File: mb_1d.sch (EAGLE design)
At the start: 57 parts, among them CON1 1013279X_AMPHENOL_2X25, CON2 1013279X_AMPHENOL_2X25, U1 TPS61040, U10 TPS610981, U2 MAX5394, U3 TPS61040, U4 74HC4050, U5 RFD77101, U6 MAX5394, U7 MAX5026EUT+T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

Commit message: Began schematic
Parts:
- added U9: HEADER_5X2_SMD_1.27MM, ck:HEADER_5X2_SMD_1.27MM
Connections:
- new net AIN2: U5.P0.01/AIN2, U9.P10
- new net AREF0: U5.P0.00/AREF0, U9.P9
- net 3.3V: now also U9.P7
- net GND: now also U9.P1
- net RESET: now also U9.P8
- net SS_POT1: now also U5.P0.07
- net SS_POT2: now also U5.P0.10
- net SS_POT3: now also U5.P0.13
- net TX_EN_M: now also U9.P2
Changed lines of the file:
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@@
 <part name="U8" library="ck" deviceset="MAX5394" device=""/>
 <part name="R13" library="SparkFun-Resistors" deviceset="RESISTOR" device="0402" value="50k"/>
+<part name="U9" library="ck" deviceset="HEADER_5X2_SMD_1.27MM" device=""/>
 </parts>
 <sheets>
@@
 <instance part="U8" gate="U1" x="-95.25" y="-35.56"/>
 <instance part="R13" gate="G$1" x="-80.01" y="-49.53" rot="R90"/>
+<instance part="U9" gate="U1" x="29.21" y="-64.77"/>
 </instances>
 <busses>
@@
 <label x="-80.01" y="-59.69" size="1.778" layer="95"/>
 </segment>
+<segment>
+<pinref part="U9" gate="U1" pin="P1"/>
+<wire x1="21.59" y1="-58.42" x2="13.97" y2="-58.42" width="0.1524" layer="91"/>
+<label x="13.97" y="-58.42" size="1.778" layer="95"/>
+</segment>
 </net>
 <net name="3.3V" class="0">
@@
 <label x="-113.03" y="-27.94" size="1.778" layer="95"/>
 </segment>
+<segment>
+<pinref part="U9" gate="U1" pin="P7"/>
+<wire x1="36.83" y1="-66.04" x2="45.72" y2="-66.04" width="0.1524" layer="91"/>
+<label x="40.64" y="-66.04" size="1.778" layer="95"/>
+</segment>
 </net>
 <net name="SCK" class="0">
@@
 <pinref part="CON2" gate="CON1" pin="P$41"/>
 </segment>
+<segment>
+<pinref part="U9" gate="U1" pin="P2"/>
+<wire x1="21.59" y1="-60.96" x2="13.97" y2="-60.96" width="0.1524" layer="91"/>
+<label x="10.16" y="-60.96" size="1.778" layer="95"/>
+</segment>
 </net>
 <net name="RSTB_M" class="0">
@@
 <wire x1="90.17" y1="-62.23" x2="83.82" y2="-62.23" width="0.1524" layer="91"/>
 <label x="83.82" y="-62.23" size="1.778" layer="95"/>
+</segment>
+<segment>
+<pinref part="U9" gate="U1" pin="P8"/>
+<wire x1="36.83" y1="-63.5" x2="45.72" y2="-63.5" width="0.1524" layer="91"/>
+<label x="40.64" y="-63.5" size="1.778" layer="95"/>
 </segment>
 </net>
@@
 <label x="12.7" y="25.4" size="1.778" layer="95"/>
 </segment>
+<segment>
+<pinref part="U5" gate="G$1" pin="P0.07"/>
+<wire x1="125.73" y1="-107.95" x2="125.73" y2="-114.3" width="0.1524" layer="91"/>
+<label x="125.73" y="-119.38" size="1.778" layer="95" rot="R90"/>
+</segment>
 </net>
 <net name="SS_POT2" class="0">
@@
 <wire x1="-224.79" y1="-36.83" x2="-233.68" y2="-36.83" width="0.1524" layer="91"/>
 <label x="-237.49" y="-36.83" size="1.778" layer="95"/>
+</segment>
+<segment>
+<pinref part="U5" gate="G$1" pin="P0.10"/>
+<wire x1="128.27" y1="-107.95" x2="128.27" y2="-114.3" width="0.1524" layer="91"/>
+<label x="128.27" y="-119.38" size="1.778" layer="95" rot="R90"/>
 </segment>
 </net>
@@
 <label x="-118.11" y="-33.02" size="1.778" layer="95"/>
 </segment>
+<segment>
+<pinref part="U5" gate="G$1" pin="P0.13"/>
+<wire x1="130.81" y1="-107.95" x2="130.81" y2="-114.3" width="0.1524" layer="91"/>
+<label x="130.81" y="-119.38" size="1.778" layer="95" rot="R90"/>
+</segment>
 </net>
 <net name="MOSI_LS" class="0">
@@
 </segment>
 </net>
+<net name="AIN2" class="0">
+<segment>
+<pinref part="U9" gate="U1" pin="P10"/>
+<wire x1="36.83" y1="-58.42" x2="45.72" y2="-58.42" width="0.1524" layer="91"/>
+<label x="41.91" y="-58.42" size="1.778" layer="95"/>
+</segment>
+<segment>
+<pinref part="U5" gate="G$1" pin="P0.01/AIN2"/>
+<wire x1="118.11" y1="-107.95" x2="118.11" y2="-114.3" width="0.1524" layer="91"/>
+<label x="118.11" y="-114.3" size="1.778" layer="95" rot="R90"/>
+</segment>
+</net>
+<net name="AREF0" class="0">
+<segment>
+<pinref part="U9" gate="U1" pin="P9"/>
+<wire x1="36.83" y1="-60.96" x2="45.72" y2="-60.96" width="0.1524" layer="91"/>
+<label x="40.64" y="-60.96" size="1.778" layer="95"/>
+</segment>
+<segment>
+<pinref part="U5" gate="G$1" pin="P0.00/AREF0"/>
+<wire x1="123.19" y1="-107.95" x2="123.19" y2="-114.3" width="0.1524" layer="91"/>
+<label x="123.19" y="-114.3" size="1.778" layer="95" rot="R90"/>
+</segment>
+</net>

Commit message: Fixed errors
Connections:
- removed net N$5: D3.C, D4.A
- removed net N$6: D4.C, D5.A
- net 3.3V: now also U5.VDD
- net GND: now also U5.GND@1, U5.GND@42, U5.GND@44, U5.GND@45
- net N$10: now also D6.C, R3.1; no longer D5.C, D6.A
- net N$4: now also D3.C, D4.A
- net N$7: now also D4.C, D5.A
- net N$9: now also D5.C, D6.A
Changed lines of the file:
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@@
 <setting verticaltext="up"/>
 </settings>
-<grid distance="0.05" unitdist="inch" unit="inch" style="lines" multiple="1" display="no" altdistance="0.01" altunitdist="inch" altunit="inch"/>
+<grid distance="0.1" unitdist="inch" unit="inch" style="lines" multiple="1" display="no" altdistance="0.01" altunitdist="inch" altunit="inch"/>
 <layers>
 <layer number="1" name="Top" color="4" fill="1" visible="no" active="no"/>
@@
 </segment>
 <segment>
-<wire x1="91.44" y1="-44.45" x2="83.82" y2="-44.45" width="0.1524" layer="91"/>
-<label x="85.09" y="-44.45" size="1.778" layer="95"/>
-</segment>
-<segment>
 <pinref part="U5" gate="G$1" pin="GND@2"/>
 <wire x1="90.17" y1="-46.99" x2="83.82" y2="-46.99" width="0.1524" layer="91"/>
@@
 </segment>
 <segment>
-<wire x1="105.41" y1="-106.68" x2="105.41" y2="-114.3" width="0.1524" layer="91"/>
-<label x="105.41" y="-113.03" size="1.778" layer="95" rot="R90"/>
-</segment>
-<segment>
 <pinref part="U5" gate="G$1" pin="GND@43"/>
 <wire x1="107.95" y1="-107.95" x2="107.95" y2="-114.3" width="0.1524" layer="91"/>
 <label x="107.95" y="-113.03" size="1.778" layer="95" rot="R90"/>
-</segment>
-<segment>
-<wire x1="135.89" y1="-106.68" x2="135.89" y2="-114.3" width="0.1524" layer="91"/>
-<label x="135.89" y="-113.03" size="1.778" layer="95" rot="R90"/>
-</segment>
-<segment>
-<wire x1="138.43" y1="-106.68" x2="138.43" y2="-114.3" width="0.1524" layer="91"/>
-<label x="138.43" y="-113.03" size="1.778" layer="95" rot="R90"/>
 </segment>
 <segment>
@@
 <label x="13.97" y="-58.42" size="1.778" layer="95"/>
 </segment>
+<segment>
+<pinref part="U5" gate="G$1" pin="GND@1"/>
+<wire x1="90.17" y1="-44.45" x2="83.82" y2="-44.45" width="0.1524" layer="91"/>
+<label x="85.09" y="-44.45" size="1.778" layer="95"/>
+</segment>
+<segment>
+<pinref part="U5" gate="G$1" pin="GND@42"/>
+<wire x1="105.41" y1="-107.95" x2="105.41" y2="-114.3" width="0.1524" layer="91"/>
+<label x="105.41" y="-113.03" size="1.778" layer="95" rot="R90"/>
+</segment>
+<segment>
+<pinref part="U5" gate="G$1" pin="GND@44"/>
+<wire x1="135.89" y1="-107.95" x2="135.89" y2="-114.3" width="0.1524" layer="91"/>
+<label x="135.89" y="-114.3" size="1.778" layer="95" rot="R90"/>
+</segment>
+<segment>
+<pinref part="U5" gate="G$1" pin="GND@45"/>
+<wire x1="138.43" y1="-107.95" x2="138.43" y2="-114.3" width="0.1524" layer="91"/>
+<label x="138.43" y="-114.3" size="1.778" layer="95" rot="R90"/>
+</segment>
 </net>
 <net name="3.3V" class="0">
@@
 <junction x="-292.1" y="-29.21"/>
 <label x="-295.91" y="-29.21" size="1.778" layer="95"/>
-</segment>
-<segment>
-<wire x1="91.44" y1="-59.69" x2="83.82" y2="-59.69" width="0.1524" layer="91"/>
-<label x="83.82" y="-59.69" size="1.778" layer="95"/>
 </segment>
 <segment>
@@
 <label x="40.64" y="-66.04" size="1.778" layer="95"/>
 </segment>
+<segment>
+<pinref part="U5" gate="G$1" pin="VDD"/>
+<wire x1="90.17" y1="-59.69" x2="83.82" y2="-59.69" width="0.1524" layer="91"/>
+<label x="85.09" y="-59.69" size="1.778" layer="95"/>
+</segment>
 </net>
 <net name="SCK" class="0">
@@
 </segment>
 </net>
-<net name="N$4" class="0">
-<segment>
-<pinref part="C7" gate="G$1" pin="2"/>
-<wire x1="-134.62" y1="31.75" x2="-134.62" y2="30.48" width="0.1524" layer="91"/>
-</segment>
-</net>
 <net name="N$7" class="0">
 <segment>
@@
 <wire x1="-115.57" y1="22.86" x2="-125.73" y2="22.86" width="0.1524" layer="91"/>
 <junction x="-125.73" y="22.86"/>
-</segment>
-</net>
-<net name="N$9" class="0">
-<segment>
-<pinref part="C9" gate="G$1" pin="2"/>
-<wire x1="-114.3" y1="31.75" x2="-114.3" y2="30.48" width="0.1524" layer="91"/>
+<pinref part="D4" gate="G$1" pin="C"/>
+<wire x1="-128.27" y1="30.48" x2="-125.73" y2="30.48" width="0.1524" layer="91"/>
+<pinref part="D5" gate="G$1" pin="A"/>
+<wire x1="-125.73" y1="30.48" x2="-123.19" y2="30.48" width="0.1524" layer="91"/>
+<junction x="-125.73" y="30.48"/>
 </segment>
 </net>
@@
 </segment>
 </net>
-<net name="N$5" class="0">
-<segment>
-<pinref part="D3" gate="G$1" pin="C"/>
-<pinref part="D4" gate="G$1" pin="A"/>
-<wire x1="-138.43" y1="30.48" x2="-133.35" y2="30.48" width="0.1524" layer="91"/>
-</segment>
-</net>
-<net name="N$6" class="0">
-<segment>
-<pinref part="D4" gate="G$1" pin="C"/>
-<pinref part="D5" gate="G$1" pin="A"/>
-<wire x1="-128.27" y1="30.48" x2="-123.19" y2="30.48" width="0.1524" layer="91"/>
-</segment>
-</net>
-<net name="N$10" class="0">
-<segment>
-<pinref part="D5" gate="G$1" pin="C"/>
-<pinref part="D6" gate="G$1" pin="A"/>
-<wire x1="-118.11" y1="30.48" x2="-113.03" y2="30.48" width="0.1524" layer="91"/>
-</segment>
-</net>
 <net name="N$12" class="0">
 <segment>
@@
 </segment>
 </net>
+<net name="N$9" class="0">
+<segment>
+<pinref part="D5" gate="G$1" pin="C"/>
+<pinref part="D6" gate="G$1" pin="A"/>
+<wire x1="-118.11" y1="30.48" x2="-114.3" y2="30.48" width="0.1524" layer="91"/>
+<pinref part="C9" gate="G$1" pin="2"/>
+<wire x1="-114.3" y1="30.48" x2="-113.03" y2="30.48" width="0.1524" layer="91"/>
+<wire x1="-114.3" y1="31.75" x2="-114.3" y2="30.48" width="0.1524" layer="91"/>
+<junction x="-114.3" y="30.48"/>
+</segment>
+</net>
+<net name="N$10" class="0">
+<segment>
+<pinref part="D6" gate="G$1" pin="C"/>
+<pinref part="R3" gate="G$1" pin="1"/>
+<wire x1="-107.95" y1="30.48" x2="-106.68" y2="30.48" width="0.1524" layer="91"/>
+</segment>
+</net>
+<net name="N$4" class="0">
+<segment>
+<pinref part="D3" gate="G$1" pin="C"/>
+<pinref part="C7" gate="G$1" pin="2"/>
+<wire x1="-138.43" y1="30.48" x2="-134.62" y2="30.48" width="0.1524" layer="91"/>
+<wire x1="-134.62" y1="30.48" x2="-134.62" y2="31.75" width="0.1524" layer="91"/>
+<pinref part="D4" gate="G$1" pin="A"/>
+<wire x1="-134.62" y1="30.48" x2="-133.35" y2="30.48" width="0.1524" layer="91"/>
+<junction x="-134.62" y="30.48"/>
+</segment>
+</net>

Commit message: Added LQH3NPN470MJRL to schematic
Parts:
- removed L2: CR32, inductors:CR32
- added C17: 470nF, SparkFun-Capacitors:470NF-0402-16V-10%
- added U$2: (no value), Personal:LQH3NPN470MJRL
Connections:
- removed net HVCMUT: R8.1, U$1.OUT
- net 3.3V: now also U$2.1; no longer L2.1
- net CLK_CP: now also U9.P4
- net GND: now also C17.1
- net HVDC: now also C17.2, R8.1, U$1.OUT
- net N$8: now also U$2.2; no longer L2.2
- net OUT16_BUF: now also U9.P5
- net REF_CLK: now also U9.P3
- net REF_CLK_BUF: now also U9.P6
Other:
- moved on the sheet: U4, U9

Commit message: Routed Simblee
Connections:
- net CLK_CP: now also U5.P0.11; no longer U5.P0.04/AIN5
- net RSTB_M: now also U5.P0.09; no longer U5.P0.06/AREF1/AIN7
- net SS_POT1: now also U5.P0.16; no longer U5.P0.07
- net SS_POT2: now also U5.P0.15; no longer U5.P0.10
- net SS_POT3: now also U5.P0.12; no longer U5.P0.13
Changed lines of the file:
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@@
 </variantdefs>
 <classes>
-<class number="0" name="default" width="0" drill="0">
+<class number="0" name="default" width="0.1524" drill="0.254">
+<clearance class="0" value="0.1524"/>
 </class>
 </classes>
@@
 </segment>
 <segment>
-<pinref part="U5" gate="G$1" pin="P0.04/AIN5"/>
-<wire x1="153.67" y1="-85.09" x2="162.56" y2="-85.09" width="0.1524" layer="91"/>
-<label x="154.94" y="-85.09" size="1.778" layer="95"/>
-</segment>
-<segment>
 <pinref part="U9" gate="U1" pin="P4"/>
 <wire x1="115.57" y1="7.62" x2="107.95" y2="7.62" width="0.1524" layer="91"/>
 <label x="105.41" y="7.62" size="1.778" layer="95"/>
+</segment>
+<segment>
+<pinref part="U5" gate="G$1" pin="P0.11"/>
+<wire x1="90.17" y1="-85.09" x2="83.82" y2="-85.09" width="0.1524" layer="91"/>
+<label x="80.01" y="-85.09" size="1.778" layer="95"/>
 </segment>
 </net>
@@
 </segment>
 <segment>
-<pinref part="U5" gate="G$1" pin="P0.06/AREF1/AIN7"/>
-<wire x1="153.67" y1="-87.63" x2="162.56" y2="-87.63" width="0.1524" layer="91"/>
-<label x="154.94" y="-87.63" size="1.778" layer="95"/>
+<pinref part="U5" gate="G$1" pin="P0.09"/>
+<wire x1="90.17" y1="-87.63" x2="83.82" y2="-87.63" width="0.1524" layer="91"/>
+<label x="81.28" y="-87.63" size="1.778" layer="95"/>
 </segment>
 </net>
@@
 </segment>
 <segment>
-<pinref part="U5" gate="G$1" pin="P0.07"/>
-<wire x1="125.73" y1="-107.95" x2="125.73" y2="-114.3" width="0.1524" layer="91"/>
-<label x="125.73" y="-119.38" size="1.778" layer="95" rot="R90"/>
+<pinref part="U5" gate="G$1" pin="P0.16"/>
+<wire x1="90.17" y1="-77.47" x2="83.82" y2="-77.47" width="0.1524" layer="91"/>
+<label x="80.01" y="-77.47" size="1.778" layer="95"/>
 </segment>
 </net>
@@
 </segment>
 <segment>
-<pinref part="U5" gate="G$1" pin="P0.10"/>
-<wire x1="128.27" y1="-107.95" x2="128.27" y2="-114.3" width="0.1524" layer="91"/>
-<label x="128.27" y="-119.38" size="1.778" layer="95" rot="R90"/>
+<pinref part="U5" gate="G$1" pin="P0.15"/>
+<wire x1="90.17" y1="-80.01" x2="83.82" y2="-80.01" width="0.1524" layer="91"/>
+<label x="80.01" y="-80.01" size="1.778" layer="95"/>
 </segment>
 </net>
@@
 </segment>
 <segment>
-<pinref part="U5" gate="G$1" pin="P0.13"/>
-<wire x1="130.81" y1="-107.95" x2="130.81" y2="-114.3" width="0.1524" layer="91"/>
-<label x="130.81" y="-119.38" size="1.778" layer="95" rot="R90"/>
-</segment>
-</net>
+<pinref part="U5" gate="G$1" pin="P0.12"/>
+<wire x1="90.17" y1="-82.55" x2="83.82" y2="-82.55" width="0.1524" layer="91"/>
+<label x="81.28" y="-82.55" size="1.778" layer="95"/>
+</segment>
+</net>

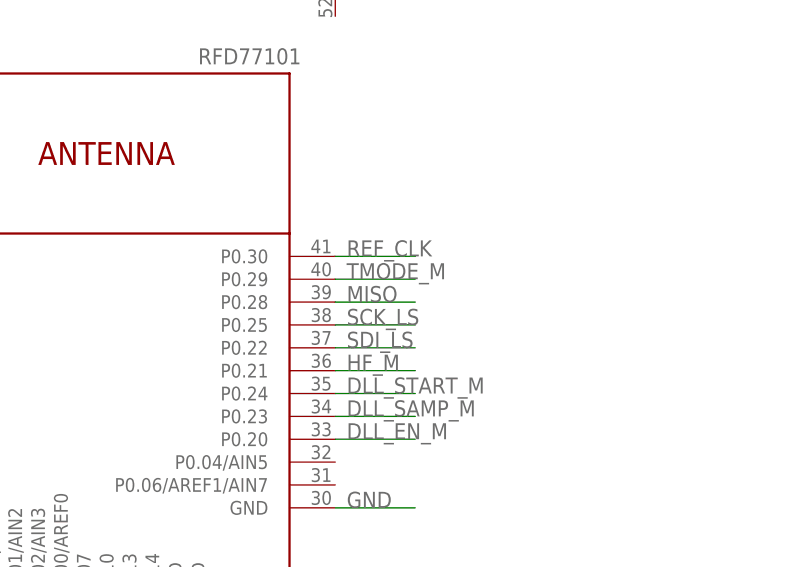
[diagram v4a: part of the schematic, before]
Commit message: Updated Simblee routes
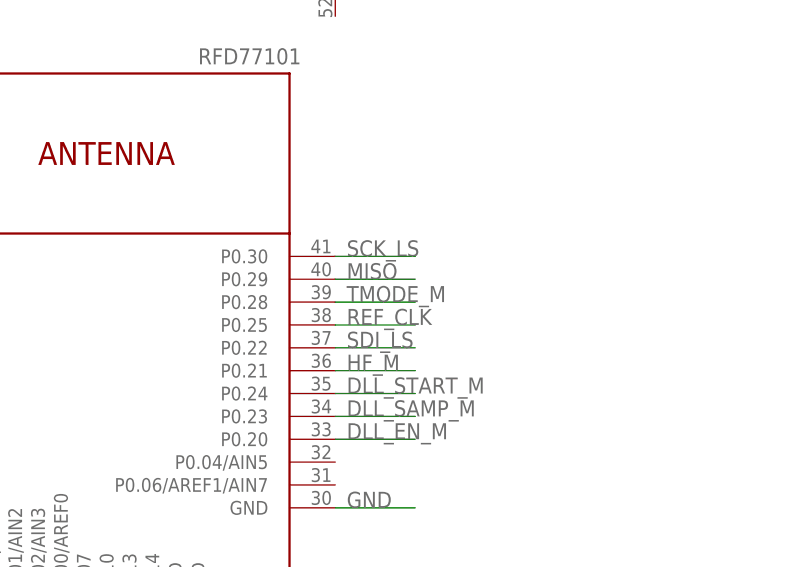
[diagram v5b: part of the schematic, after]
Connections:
- net MISO: now also U5.P0.29; no longer U5.P0.28
- net REF_CLK: now also U5.P0.25; no longer U5.P0.30
- net SCK_LS: now also U5.P0.30; no longer U5.P0.25
- net TMODE_M: now also U5.P0.28; no longer U5.P0.29

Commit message: First version of completed routing
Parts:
- removed D2: ZHCS1000, zetex:ZHCS1000
- removed U4: 74HC4050, ck:74HC4050
- added U$3: (no value), Personal:SN74AUP2G34DCKR
- added U$4: (no value), Personal:DB2J40700L
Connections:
- removed net MOSI_LS: U2.DIN, U4.3Y, U6.DIN, U8.DIN
- removed net N$3: C6.1, D2.K, D3.A
- removed net N$8: C7.1, C9.1, D2.A, U$2.2, U7.LX
- new net DIODE1: C6.1, D3.A, U$4.1
- new net DIODE2: C7.1, C9.1, U$2.2, U$4.2, U7.LX
- net CLK_CP: now also U5.P0.08; no longer U5.P0.11
- net DLL_START_M: now also U5.P0.30; no longer U5.P0.24
- net GND: now also U$3.GND; no longer U4.GND
- net HF_M: now also U5.P0.29; no longer U5.P0.21
- net MISO: now also U5.P0.28; no longer U5.P0.29
- net MOSI: now also U$3.2A, U2.DIN, U5.P0.21, U6.DIN, U8.DIN; no longer U4.2A
- net OUT16_BUF: now also U5.P0.14; no longer U5.P0.19
- net REF_CLK: now also U5.P0.22; no longer U5.P0.25
- net REF_CLK_BUF: now also U5.P0.13; no longer U5.P0.17
- net SCK: now also U$3.1A, U2.SCLK, U5.P0.24, U6.SCLK, U8.SCLK; no longer U4.1A
- net SCK_LS: now also U$3.1Y; no longer U2.SCLK, U4.1Y, U5.P0.30, U6.SCLK, U8.SCLK
- net SDI_LS: now also U$3.2Y; no longer U4.2Y, U5.P0.22
- net SS_POT1: now also U5.P0.19; no longer U5.P0.16
- net TMODE_M: now also U5.P0.25; no longer U5.P0.28
- net VDD: now also U$3.VCC; no longer U4.VCC

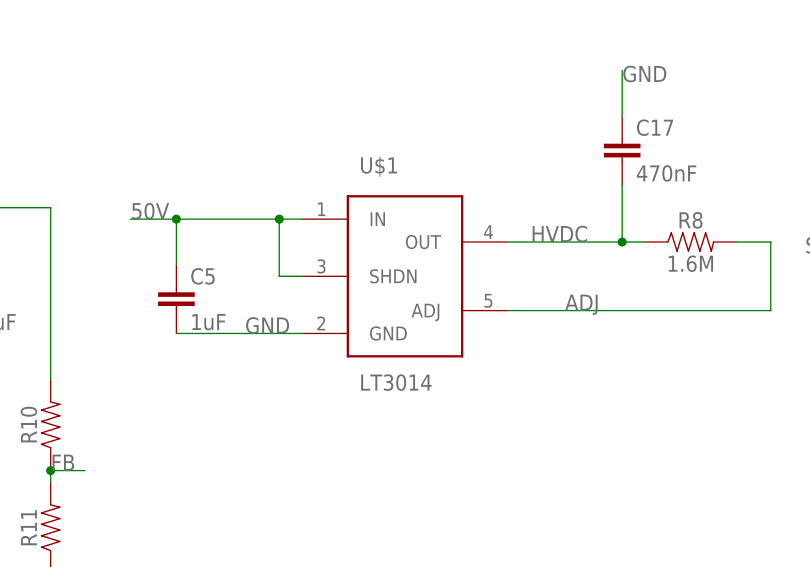
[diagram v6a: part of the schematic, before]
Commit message: Fixed LT3014 error
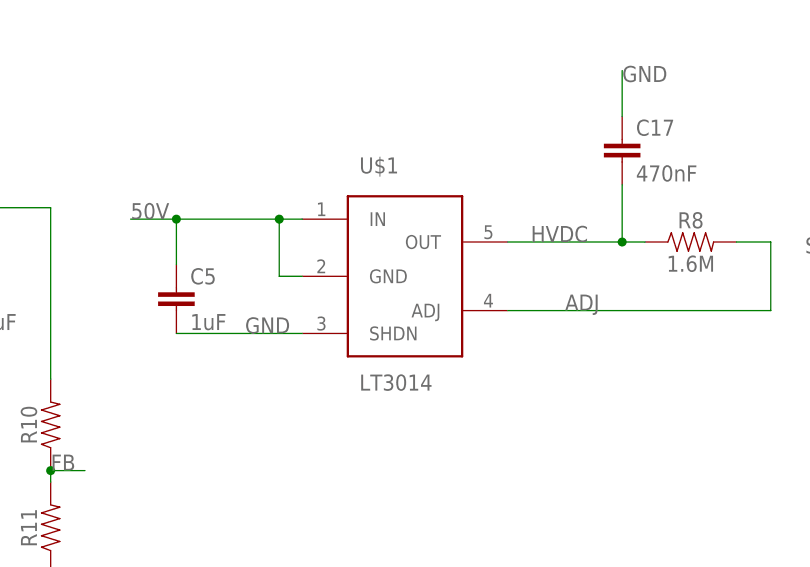
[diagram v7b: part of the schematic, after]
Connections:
- net 50V: now also U$1.GND; no longer U$1.SHDN
- net GND: now also U$1.SHDN; no longer U$1.GND
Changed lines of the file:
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@@
 </segment>
 <segment>
-<pinref part="U$1" gate="G$1" pin="GND"/>
+<pinref part="U$1" gate="G$1" pin="SHDN"/>
 <wire x1="-43.18" y1="16.51" x2="-57.15" y2="16.51" width="0.1524" layer="91"/>
 <pinref part="C5" gate="G$1" pin="2"/>
@@
 <pinref part="U$1" gate="G$1" pin="IN"/>
 <wire x1="-43.18" y1="29.21" x2="-45.72" y2="29.21" width="0.1524" layer="91"/>
-<pinref part="U$1" gate="G$1" pin="SHDN"/>
+<pinref part="U$1" gate="G$1" pin="GND"/>
 <wire x1="-43.18" y1="22.86" x2="-45.72" y2="22.86" width="0.1524" layer="91"/>
 <wire x1="-45.72" y1="22.86" x2="-45.72" y2="29.21" width="0.1524" layer="91"/>
